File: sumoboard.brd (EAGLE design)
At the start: 50 x 46 mm, 27 parts

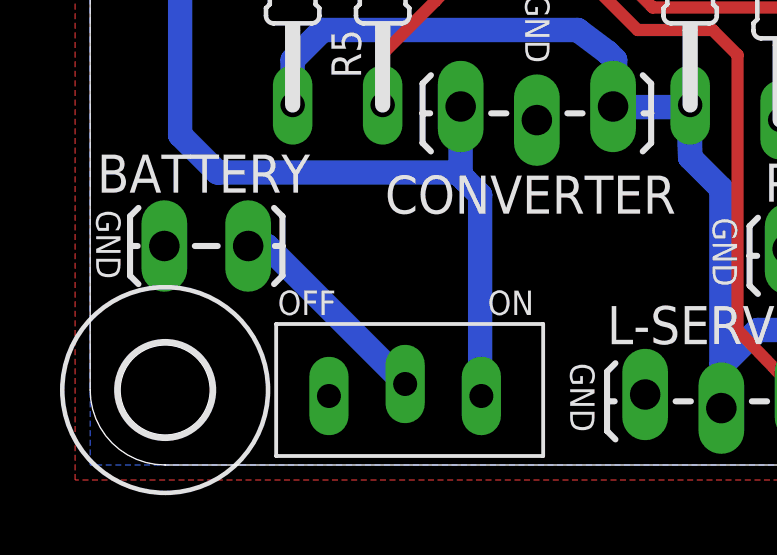
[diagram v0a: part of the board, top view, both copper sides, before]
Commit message: updated sumoboard
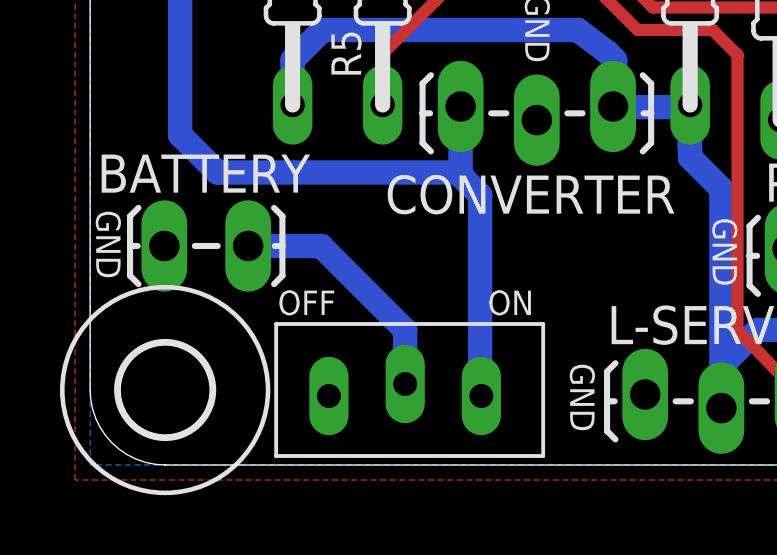
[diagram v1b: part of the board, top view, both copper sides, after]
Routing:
- net BAT_IN: track 7.14 -> 8.19 mm
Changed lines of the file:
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@@
 <?xml version="1.0" encoding="utf-8"?>
 <!DOCTYPE eagle SYSTEM "eagle.dtd">
-<eagle version="7.1.0">
+<eagle version="6.5.0">
 <drawing>
 <settings>
@@
 <setting verticaltext="up"/>
 </settings>
-<grid distance="0.25" unitdist="mm" unit="mm" style="lines" multiple="1" display="yes" altdistance="0.5" altunitdist="mm" altunit="mm"/>
+<grid distance="0.5" unitdist="mm" unit="mm" style="lines" multiple="1" display="yes" altdistance="0.5" altunitdist="mm" altunit="mm"/>
 <layers>
 <layer number="1" name="Top" color="4" fill="1" visible="yes" active="yes"/>
@@
 <text x="14.5" y="15.7" size="0.8128" layer="21" rot="SR270">GND</text>
 <text x="0.2" y="8.5" size="0.8128" layer="21" rot="SR270">GND</text>
+<dimension x1="2.5" y1="43.5" x2="2.5" y2="2.5" x3="-6.5" y3="23" textsize="1.778" layer="16"/>
+<dimension x1="2.5" y1="2.5" x2="47.5" y2="2.5" x3="25" y3="-5.5" textsize="1.778" layer="16"/>
 </plain>
 <attributes>
@@
 <pass name="Default">
 <param name="RoutingGrid" value="50mil"/>
-<param name="AutoGrid" value="1"/>
-<param name="Efforts" value="0"/>
-<param name="TopRouterVariant" value="1"/>
 <param name="tpViaShape" value="round"/>
-<param name="PrefDir.1" value="a"/>
+<param name="PrefDir.1" value="|"/>
 <param name="PrefDir.2" value="0"/>
 <param name="PrefDir.3" value="0"/>
@@
 <param name="PrefDir.14" value="0"/>
 <param name="PrefDir.15" value="0"/>
-<param name="PrefDir.16" value="a"/>
+<param name="PrefDir.16" value="-"/>
 <param name="cfVia" value="8"/>
 <param name="cfNonPref" value="5"/>
@@
 <signal name="BAT_IN">
 <contactref element="POWER" pad="COMMON"/>
-<wire x1="5.9" y1="7.3" x2="10.5" y2="2.7" width="0.8128" layer="16"/>
 <contactref element="BATTERY" pad="2"/>
-<wire x1="5.267" y1="7.3" x2="5.9" y2="7.3" width="0.8128" layer="16"/>
+<wire x1="5.267" y1="7.3" x2="7.7" y2="7.3" width="0.8128" layer="16"/>
+<wire x1="7.7" y1="7.3" x2="10.5" y2="4.5" width="0.8128" layer="16"/>
+<wire x1="10.5" y1="4.5" x2="10.5" y2="2.7" width="0.8128" layer="16"/>
 </signal>
 </signals>

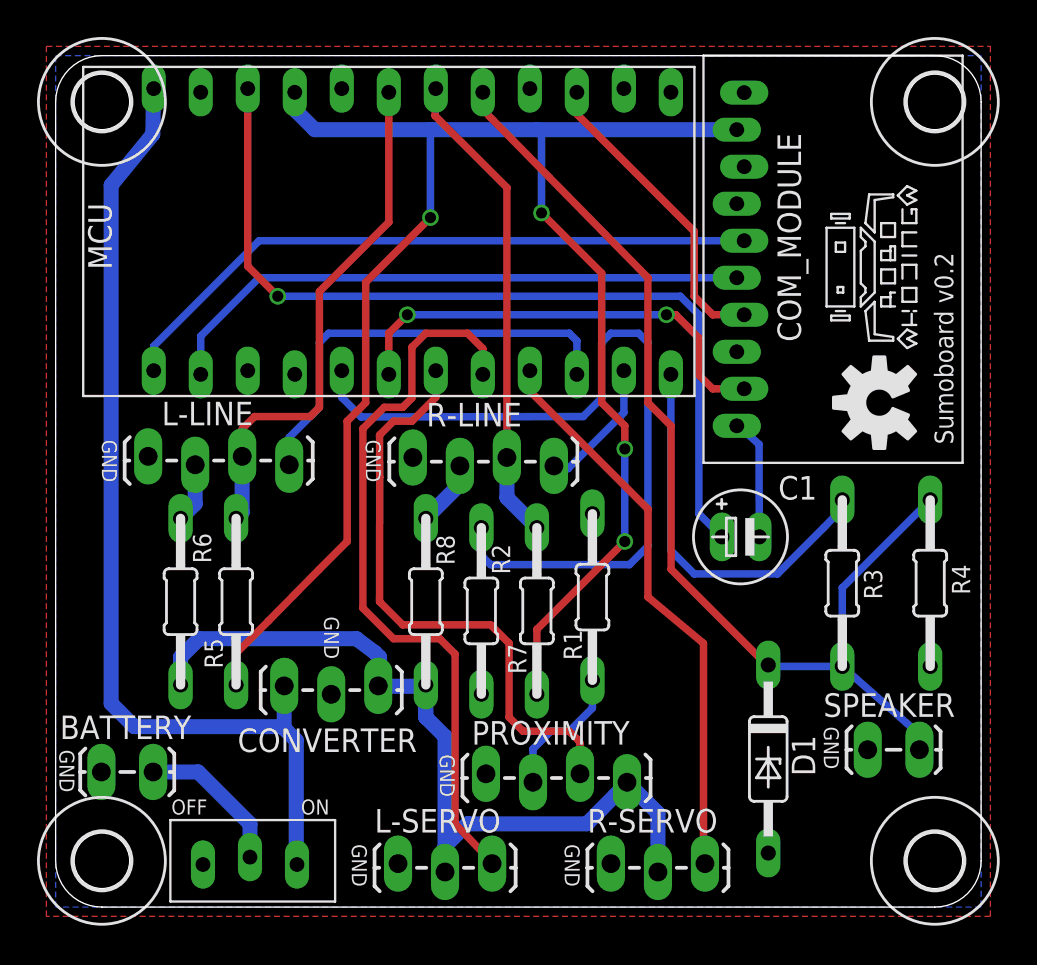
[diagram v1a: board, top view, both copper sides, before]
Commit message: updated sumoboard
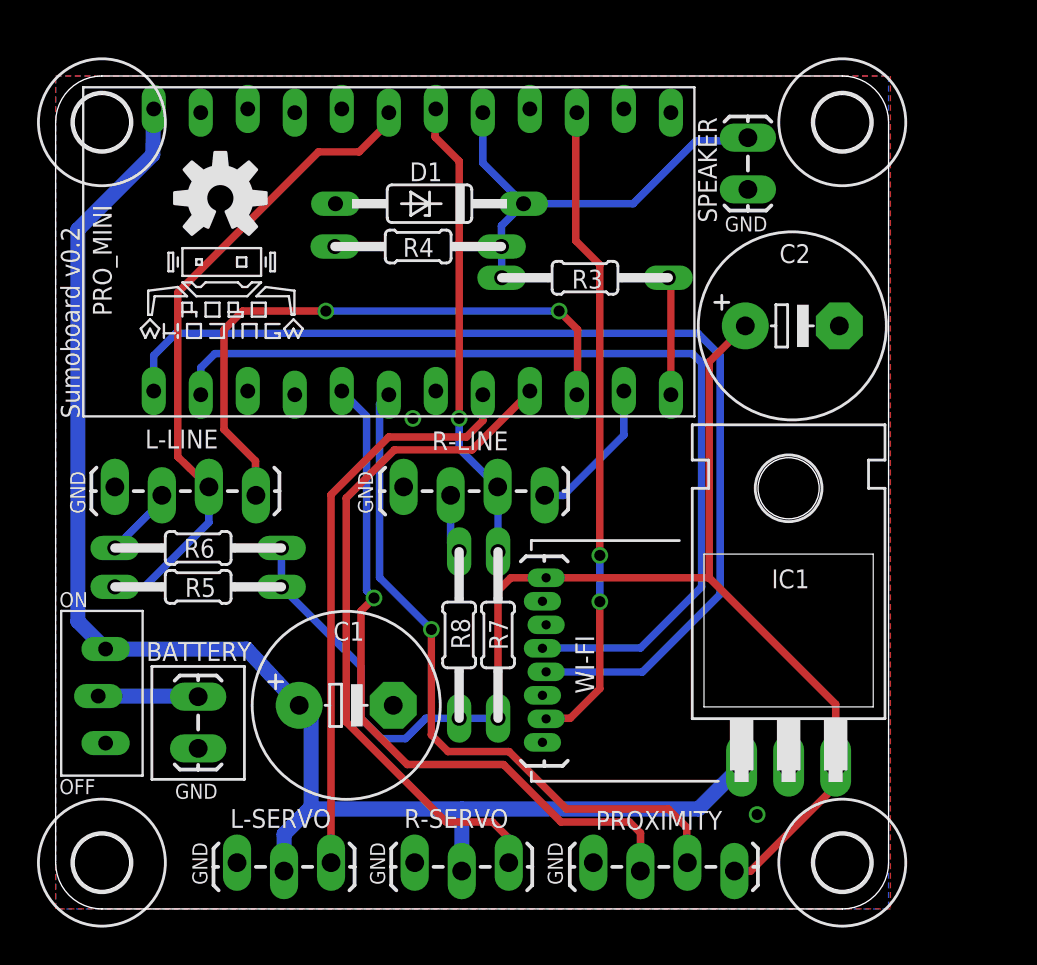
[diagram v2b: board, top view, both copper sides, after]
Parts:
- removed COM_MODULE: (no value), usr_wifi:WIFI_MODULE-T
- removed CONVERTER: (no value), SparkFun-Connectors:1X03_LOCK_LONGPADS
- removed MCU: (no value), SparkFun-Boards:ARDUINO_PRO_MINI
- removed R1: 1K8, Child-Friendly-Parts:0204/5
- removed R2: 3K3, Child-Friendly-Parts:0204/5
- added C2: (no value), rcl:E5-10,5
- added IC1: 7805T, linear:TO220H
- added PRO_MINI: (no value), SparkFun-Boards:ARDUINO_PRO_MINI
- added WI-FI: (no value), SparkFun-Connectors:1X08_LOCK_LONGPADS
- C1: value 2.2uF -> (none); device Child-Friendly-Parts:E2-5 -> rcl:E5-10,5
- moved LOGO1 37.3 mm to (8.90, 38.3), turned to 0 degrees
- moved LOGO2 35.4 mm to (8.90, 33.0), turned to 0 degrees
- moved D1 35.1 mm to (20.2, 38.0), turned to 180 degrees
- moved R4 33.1 mm to (19.6, 35.7), turned to 180 degrees
- moved SPEAKER 31.1 mm to (37.4, 38.9), turned to 90 degrees
- moved C1 23.2 mm to (15.7, 10.9)
- moved R3 21.6 mm to (28.6, 34.0), turned to 180 degrees
- moved POWER 12.0 mm to (2.50, 11.4), turned to 90 degrees
- moved R-SERVO 10.6 mm to (19.4, 2.30)
- moved L-SERVO 8.70 mm to (9.80, 2.30)
- moved PROXIMITY 7.53 mm to (29.1, 2.30)
- moved BATTERY 5.29 mm to (7.70, 8.70), turned to 90 degrees
- moved U$2 5.12 mm to (42.5, 42.4)
- moved U$1 5.00 mm to (42.5, 2.40)
- moved R6 3.05 mm to (7.70, 19.4), turned to 0 degrees
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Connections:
- removed net +5V: CONVERTER.3, L-SERVO.2, PROXIMITY.4, R-SERVO.2, R6.2, R8.2
- removed net D4: MCU.7, PROXIMITY.3
- removed net N$1: PROXIMITY.2, R1.1
- removed net NLINK: C1.-, COM_MODULE.PWM_1
- removed net RST: C1.+, MCU.22
- net +3V3: now also C2.+, IC1.3, PROXIMITY.4, R6.2, R8.2, WI-FI.8; no longer COM_MODULE.+3V3, MCU.21
- net A0: now also PRO_MINI.17; no longer MCU.17
- net A1: now also PRO_MINI.18; no longer MCU.18
- net A2: now also PRO_MINI.19; no longer MCU.19
- net D12: now also PRO_MINI.15, WI-FI.2; no longer COM_MODULE.PWR_SW, MCU.15
- net D2: now also PROXIMITY.2, PRO_MINI.5; no longer MCU.5, R1.2, R2.1
- net D3: now also PROXIMITY.3, PRO_MINI.6; no longer COM_MODULE.PWM_2, MCU.6
- net D5: now also PRO_MINI.8; no longer MCU.8
- net D6: now also PRO_MINI.9; no longer MCU.9
- net D7: now also PRO_MINI.10; no longer MCU.10
- net D8: now also PRO_MINI.11; no longer MCU.11
- net D9: now also PRO_MINI.12; no longer MCU.12
- net GND: now also C1.-, C2.-, IC1.2, PRO_MINI.23, PRO_MINI.4, WI-FI.1; no longer COM_MODULE.GND, CONVERTER.2, MCU.23, MCU.4, R2.2
- net RXD: now also PRO_MINI.2, WI-FI.5; no longer COM_MODULE.TX, MCU.2
- net TXD: now also PRO_MINI.1, WI-FI.4; no longer COM_MODULE.RX, MCU.1
- net VIN: now also C1.+, IC1.1, L-SERVO.2, PRO_MINI.24, R-SERVO.2; no longer CONVERTER.1, MCU.24
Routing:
- net +5V: track 47.7 -> 0.00 mm
- net RST: track 47.6 -> 0.00 mm, vias 1 -> 0
- net A0: track 58.8 -> 23.9 mm
- net D4: track 32.3 -> 0.00 mm
- net VIN: track 53.9 -> 80.7 mm
- net TXD: track 35.5 -> 57.6 mm
- net +3V3: track 94.1 -> 73.8 mm, vias 4 -> 0
- net RXD: track 32.4 -> 51.1 mm
- net D12: track 16.8 -> 35.3 mm, vias 0 -> 2
- net D9: track 21.2 -> 6.38 mm
- net D3: track 24.7 -> 37.5 mm, vias 2 -> 1
- net D7: track 23.4 -> 33.2 mm, vias 0 -> 2
- net D2: track 47.1 -> 38.4 mm, vias 0 -> 1
- net D5: track 39.8 -> 31.1 mm
- net N$1: track 7.42 -> 0.00 mm
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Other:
- board size 50 x 46 mm -> 45 x 45 mm

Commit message: updated component locations
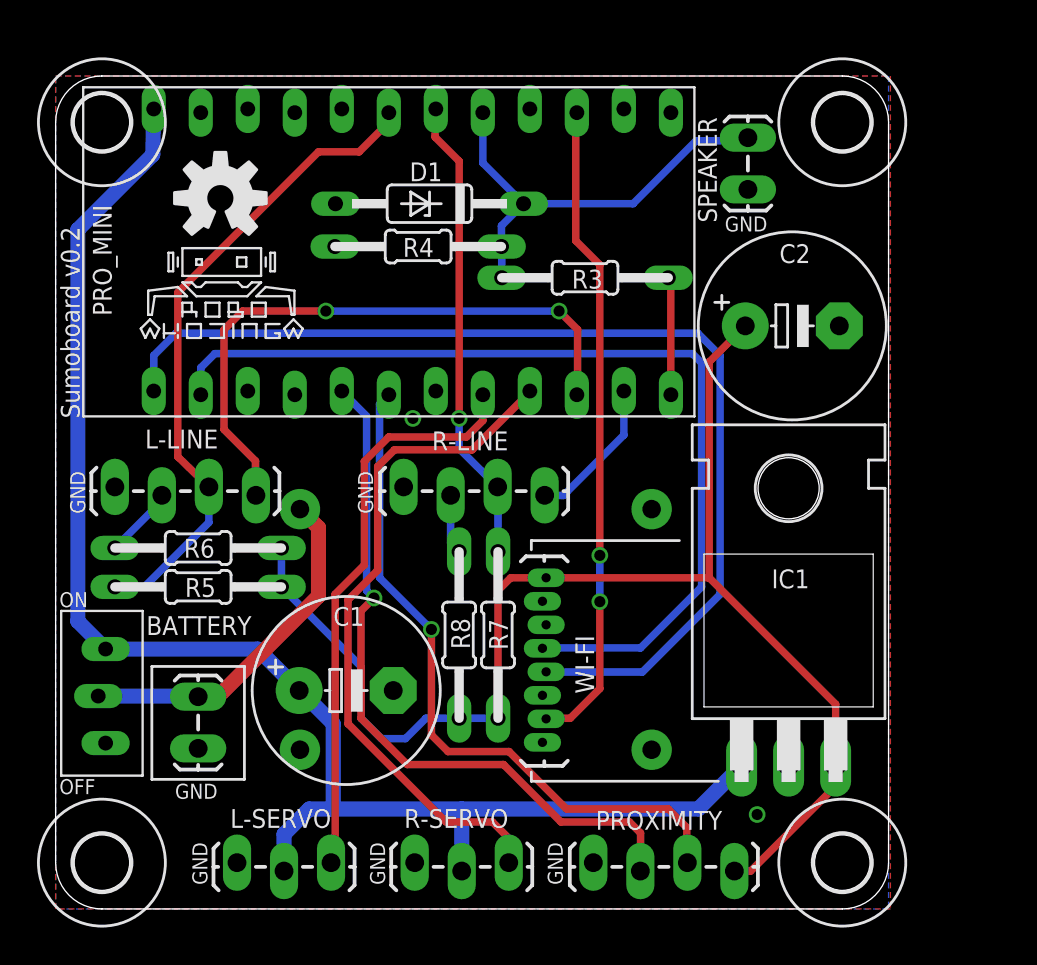
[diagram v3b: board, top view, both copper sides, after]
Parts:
- moved C1 0.80 mm to (15.7, 11.7)
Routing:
- net N$1: track 0.00 -> 13.9 mm, vias 0 -> 1
- net VIN: track 80.7 -> 81.7 mm
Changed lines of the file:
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@@
 <wire x1="10.2" y1="6.9" x2="5.2" y2="6.9" width="0.15" layer="21"/>
 <wire x1="5.2" y1="6.9" x2="5.2" y2="13" width="0.15" layer="21"/>
+<wire x1="11.7" y1="23" x2="33.7" y2="23" width="0.15" layer="22"/>
+<wire x1="33.7" y1="23" x2="33.7" y2="7" width="0.15" layer="22"/>
+<wire x1="33.7" y1="7" x2="11.7" y2="7" width="0.15" layer="22"/>
+<wire x1="11.7" y1="7" x2="11.7" y2="23" width="0.15" layer="22"/>
 </plain>
 <attributes>
@@
 <element name="U$4" library="holes" package="3,0" value="" x="2.5" y="42.4" smashed="yes"/>
 <element name="BATTERY" library="SparkFun-Connectors" package="1X02_LOCK_LONGPADS" value="" x="7.7" y="8.7" smashed="yes" rot="R90">
-<attribute name="NAME" x="4.9" y="13.3" size="1.016" layer="25" ratio="10"/>
+<attribute name="NAME" x="4.9" y="14.7" size="1.016" layer="25" ratio="10"/>
 <attribute name="VALUE" x="11.002" y="7.43" size="1.27" layer="27" font="vector" rot="R90"/>
 </element>
@@
 <attribute name="NAME" x="40.722" y="18.239" size="1.016" layer="25" ratio="10" rot="R180"/>
 </element>
-<element name="C1" library="rcl" package="E5-10,5" value="" x="15.7" y="10.9" smashed="yes">
-<attribute name="NAME" x="15.002" y="14.394" size="1.016" layer="25" ratio="10"/>
-<attribute name="VALUE" x="13.414" y="7.852" size="1.27" layer="27" ratio="10"/>
+<element name="C1" library="rcl" package="E5-10,5" value="" x="15.7" y="11.7" smashed="yes">
+<attribute name="NAME" x="15.002" y="15.194" size="1.016" layer="25" ratio="10"/>
+<attribute name="VALUE" x="13.414" y="8.652" size="1.27" layer="27" ratio="10"/>
 </element>
 <element name="C2" library="rcl" package="E5-10,5" value="" x="39.8" y="31.4" smashed="yes">
@@
 <wire x1="23.08" y1="26.28" x2="22.2" y2="25.4" width="0.4064" layer="1"/>
 <wire x1="22.2" y1="25.4" x2="18" y2="25.4" width="0.4064" layer="1"/>
-<wire x1="18" y1="25.4" x2="14.88" y2="22.28" width="0.4064" layer="1"/>
-<wire x1="14.88" y1="22.28" x2="14.88" y2="2.4" width="0.4064" layer="1"/>
+<wire x1="18" y1="25.4" x2="16.68" y2="24.08" width="0.4064" layer="1"/>
+<wire x1="16.68" y1="24.08" x2="16.68" y2="18.48" width="0.4064" layer="1"/>
+<wire x1="16.68" y1="18.48" x2="15.1" y2="16.9" width="0.4064" layer="1"/>
+<wire x1="15.1" y1="16.9" x2="15.1" y2="2.62" width="0.4064" layer="1"/>
+<wire x1="15.1" y1="2.62" x2="14.88" y2="2.4" width="0.4064" layer="1"/>
 </signal>
 <signal name="D6">
@@
 <wire x1="25.62" y1="27.82" x2="22.5" y2="24.7" width="0.4064" layer="1"/>
 <wire x1="22.5" y1="24.7" x2="18.3" y2="24.7" width="0.4064" layer="1"/>
-<wire x1="18.3" y1="24.7" x2="15.7" y2="22.1" width="0.4064" layer="1"/>
+<wire x1="18.3" y1="24.7" x2="17.4" y2="23.8" width="0.4064" layer="1"/>
 <wire x1="21.1" y1="4.6" x2="23.6" y2="4.6" width="0.4064" layer="1"/>
 <wire x1="23.6" y1="4.6" x2="24.48" y2="3.72" width="0.4064" layer="1"/>
 <wire x1="24.48" y1="3.72" x2="24.48" y2="2.4" width="0.4064" layer="1"/>
-<wire x1="21.1" y1="4.6" x2="15.7" y2="10" width="0.4064" layer="1"/>
-<wire x1="15.7" y1="10" x2="15.7" y2="22.1" width="0.4064" layer="1"/>
+<wire x1="21.1" y1="4.6" x2="15.8" y2="9.9" width="0.4064" layer="1"/>
+<wire x1="15.8" y1="9.9" x2="15.8" y2="16.6" width="0.4064" layer="1"/>
+<wire x1="15.8" y1="16.6" x2="17.4" y2="18.2" width="0.4064" layer="1"/>
+<wire x1="17.4" y1="18.2" x2="17.4" y2="23.8" width="0.4064" layer="1"/>
 </signal>
 <signal name="D7">
@@
 <contactref element="IC1" pad="1"/>
 <contactref element="C1" pad="+"/>
-<wire x1="13.7" y1="5.3" x2="13.8" y2="5.3" width="0.8128" layer="16"/>
-<wire x1="13.8" y1="5.3" x2="21.94" y2="5.3" width="0.8128" layer="16"/>
+<wire x1="13.7" y1="5.3" x2="14.9" y2="5.3" width="0.8128" layer="16"/>
+<wire x1="14.9" y1="5.3" x2="21.94" y2="5.3" width="0.8128" layer="16"/>
 <wire x1="21.94" y1="5.3" x2="34.72" y2="5.3" width="0.8128" layer="16"/>
 <wire x1="34.72" y1="5.3" x2="37.06" y2="7.64" width="0.8128" layer="16"/>
@@
 <wire x1="1.2" y1="36.6" x2="5.25" y2="40.65" width="0.8128" layer="16"/>
 <wire x1="1.2" y1="15.44" x2="2.7" y2="13.94" width="0.8128" layer="16"/>
-<wire x1="2.7" y1="13.94" x2="10.32" y2="13.94" width="0.8128" layer="16"/>
+<wire x1="2.7" y1="13.94" x2="10.92" y2="13.94" width="0.8128" layer="16"/>
 <wire x1="13.7" y1="5.3" x2="12.34" y2="3.94" width="0.8128" layer="16"/>
 <wire x1="12.34" y1="3.94" x2="12.34" y2="1.946" width="0.8128" layer="16"/>
-<wire x1="13.16" y1="10.9" x2="10.32" y2="13.94" width="0.8128" layer="16"/>
-<wire x1="13.16" y1="10.9" x2="13.8" y2="10.26" width="0.8128" layer="16"/>
-<wire x1="13.8" y1="10.26" x2="13.8" y2="5.3" width="0.8128" layer="16"/>
+<wire x1="10.92" y1="13.94" x2="13.16" y2="11.7" width="0.8128" layer="16"/>
+<wire x1="13.16" y1="11.7" x2="13.2" y2="11.7" width="0.8128" layer="16"/>
+<wire x1="13.2" y1="11.7" x2="15" y2="9.9" width="0.8128" layer="16"/>
+<wire x1="15" y1="9.9" x2="15" y2="5.4" width="0.8128" layer="16"/>
+<wire x1="15" y1="5.4" x2="14.9" y2="5.3" width="0.8128" layer="16"/>
 </signal>
 <signal name="+3V3">
@@
 <via x="19.3" y="26.4" extent="1-16" drill="0.6"/>
 <via x="37.9" y="5" extent="1-16" drill="0.6"/>
+<via x="13.2" y="8.5" extent="1-16" drill="1" diameter="2.1844" shape="square"/>
+<via x="32.2" y="8.5" extent="1-16" drill="1" diameter="2.1844" shape="square"/>
 </signal>
 <signal name="TXD">
@@
 <wire x1="17.5" y1="17.8" x2="20.3" y2="15" width="0.4064" layer="16"/>
 </signal>
+<signal name="N$1">
+<via x="13.2" y="21.5" extent="1-16" drill="1" diameter="2.1844" shape="square"/>
+<wire x1="13.2" y1="21.5" x2="14.2" y2="20.5" width="0.8128" layer="1"/>
+<wire x1="14.2" y1="20.5" x2="14.2" y2="16.8" width="0.8128" layer="1"/>
+<wire x1="14.2" y1="16.8" x2="8.7" y2="11.3" width="0.8128" layer="1"/>
+<wire x1="8.7" y1="11.3" x2="7.7" y2="11.3" width="0.8128" layer="1"/>
+</signal>
+<signal name="N$2">
+<via x="32.2" y="21.5" extent="1-16" drill="1" diameter="2.1844" shape="square"/>
+</signal>
 </signals>
